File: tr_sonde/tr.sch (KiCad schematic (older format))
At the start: 94 parts, among them J1 SMA, J2 SMA, J3 SMA, K1 SMDHDR, K2 SMDHDR, K3 SMDHDR, Q3 STD2NK90ZT4, Q4 STD2NK90ZT4, U1 L6388E, U2 75451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

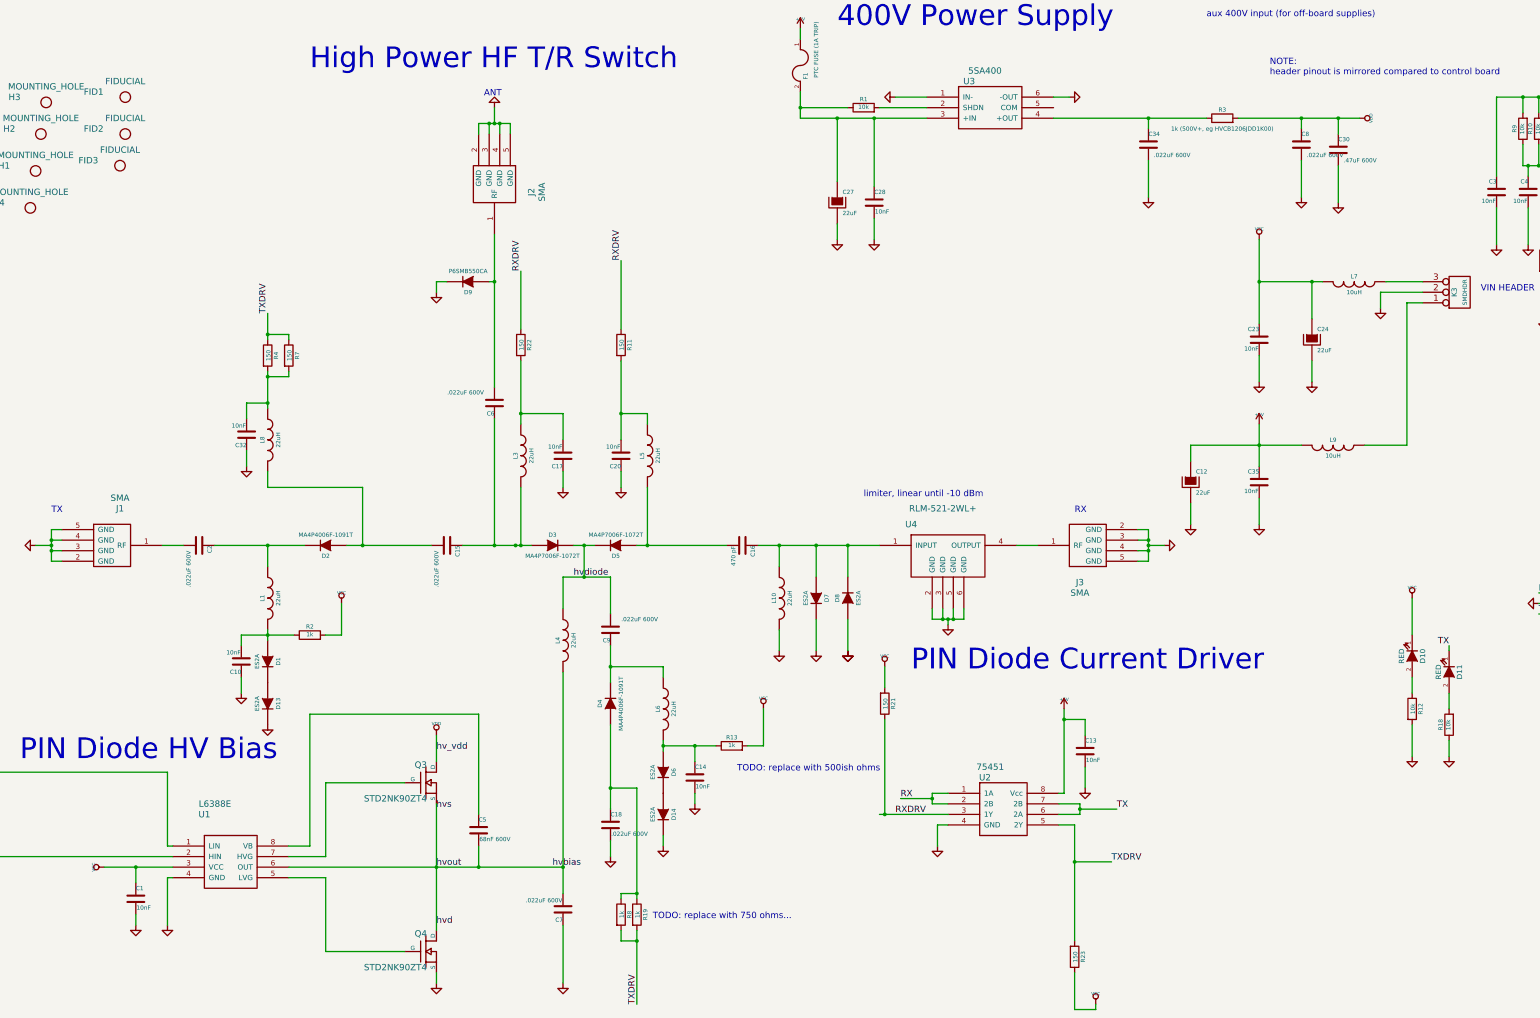
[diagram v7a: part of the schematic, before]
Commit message: updated hptr board with field modifications - switched low voltage PIN diode driver to SN75372
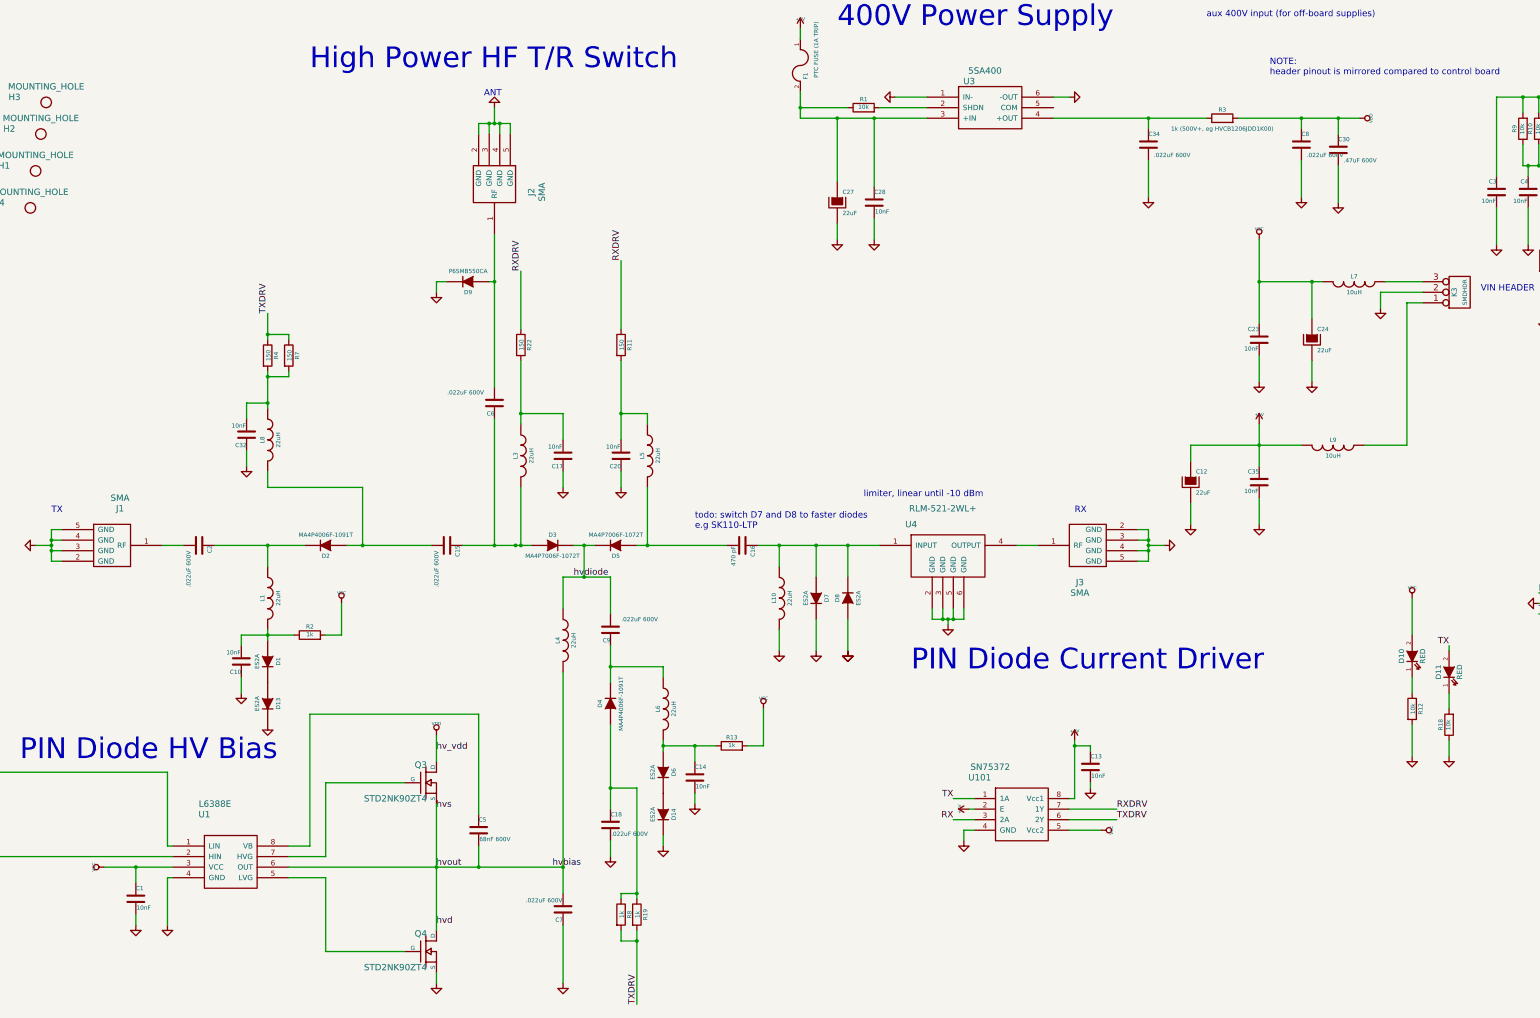
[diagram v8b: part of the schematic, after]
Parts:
- removed FID1, FID2, FID3: FIDUCIAL, sdtransmitter:FID_1MM, symbol MOUNTING_HOLE
- removed R21, R23: 150, Resistors_SMD:R_2512, symbol R
- removed U2: 75451, SOIC_Packages:SOIC-8_N, symbol 7545x
- added U101: SN75372, Housings_SOIC:SOIC-8_3.9x4.9mm_Pitch1.27mm, symbol SN75372
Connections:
- net +5V: now also U101.2 (E), U101.8 (Vcc1)
- net GND: now also U101.4 (GND)
- net RX: now also U101.3 (2A)
- net RXDRV: now also U101.7 (1Y)
- net TX: now also D11.2 (A), U101.1 (1A); no longer D11.1 (K)
- net TXDRV: now also U101.6 (2Y)
- net VCC: now also D10.2 (A), U101.5 (Vcc2); no longer D10.1 (K)
- net at R12.1: now also D10.1 (K); no longer D10.2 (A)
- net at R18.2: now also D11.1 (K); no longer D11.2 (A)
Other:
- note added: "todo: switch D7 and D8 to faster diodes\ne.g SK110-LTP"
- note removed: "TODO: replace with 500ish ohms\n"
- note removed: "TODO: replace with 750 ohms..."
- moved on the sheet: C13
